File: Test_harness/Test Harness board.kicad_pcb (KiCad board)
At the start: 4 copper layers, 233 x 160 mm, 173 parts, among them U1 TCA9548APWR

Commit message: more fixes
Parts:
- RNL2_2_1: value R_Pack04 -> 1kΩ
- moved U1 23.8 mm to (152.5, 85.7), turned to 180 degrees
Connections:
- U1 pad 4: /SCL_1 -> /SDA_0
- UL1 pad 12: /Left connector/SCL -> /SCL_0
- UL1 pad 13: /Left connector/SDA -> /SDA_0
- UL2 pad 12: /Left connector/SCL -> /SCL_0
- UL2 pad 13: /Left connector/SDA -> /SDA_0
- UL3 pad 12: /Left connector/SCL -> /SCL_0
- UL3 pad 13: /Left connector/SDA -> /SDA_0
- UL4 pad 12: /Left connector/SCL -> /SCL_0
- UL4 pad 13: /Left connector/SDA -> /SDA_0
- UL5 pad 12: /Left connector/SCL -> /SCL_0
- UL5 pad 13: /Left connector/SDA -> /SDA_0
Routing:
- net /SCL_0: track 0.00 -> 103.7 mm, vias 0 -> 8
- net /Left connector/SCL: track 103.7 -> 0.00 mm, vias 8 -> 0
- net /SDA_0: track 0.00 -> 94.8 mm, vias 0 -> 5
- net /Left connector/SDA: track 94.8 -> 0.00 mm, vias 5 -> 0
- net /Left connector/D__STOP_CLK: track 39.2 -> 93.9 mm
- net /Left connector/D__RESET: track 41.6 -> 95.6 mm
- net /Left connector/D_MEMORY: track 44.2 -> 97.4 mm
- net /Left connector/D_MEMREF: track 46.8 -> 99.2 mm
- net /Left connector/D_IR1: track 50.6 -> 102.1 mm
- net /Left connector/D_IR2: track 53.5 -> 104.3 mm
- net /Left connector/D_IR3: track 55.8 -> 105.8 mm
- net /Left connector/D_XL_MDR_HI: track 58.2 -> 107.4 mm
- net /Left connector/D__PSEL1: track 60.0 -> 108.4 mm
- net /Left connector/D__RD: track 59.7 -> 107.2 mm
- net /Left connector/D__WR: track 58.9 -> 105.8 mm
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
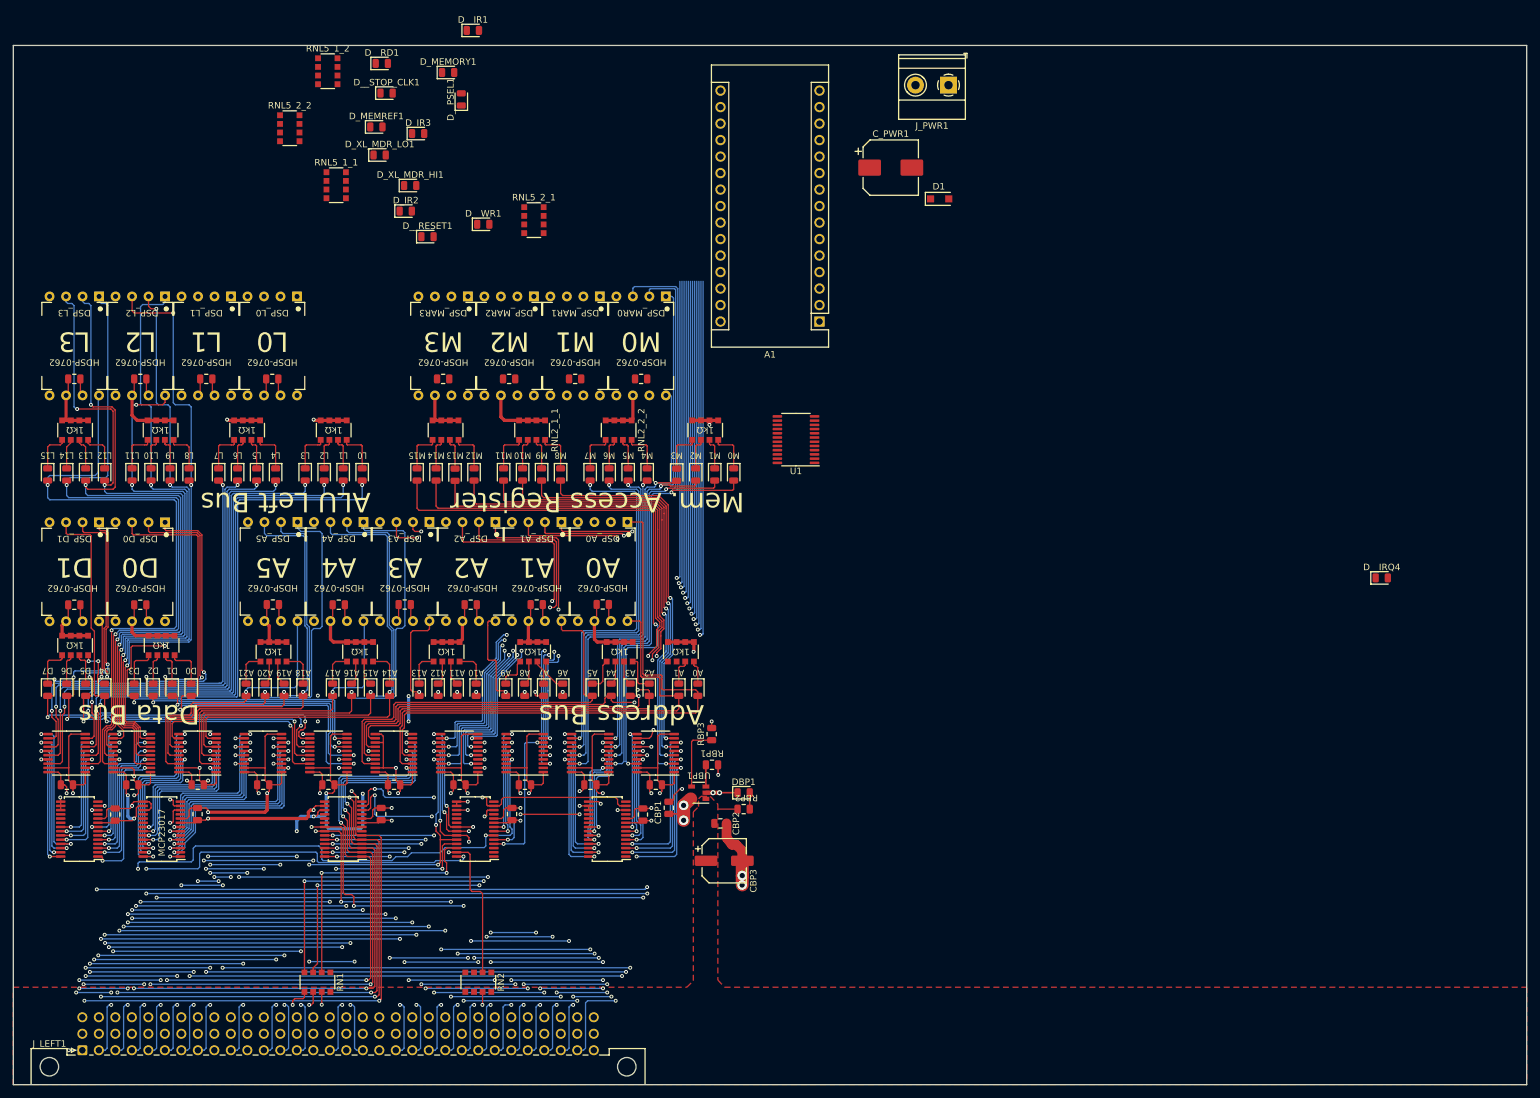
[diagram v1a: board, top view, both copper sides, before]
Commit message: position the last leds of the left side
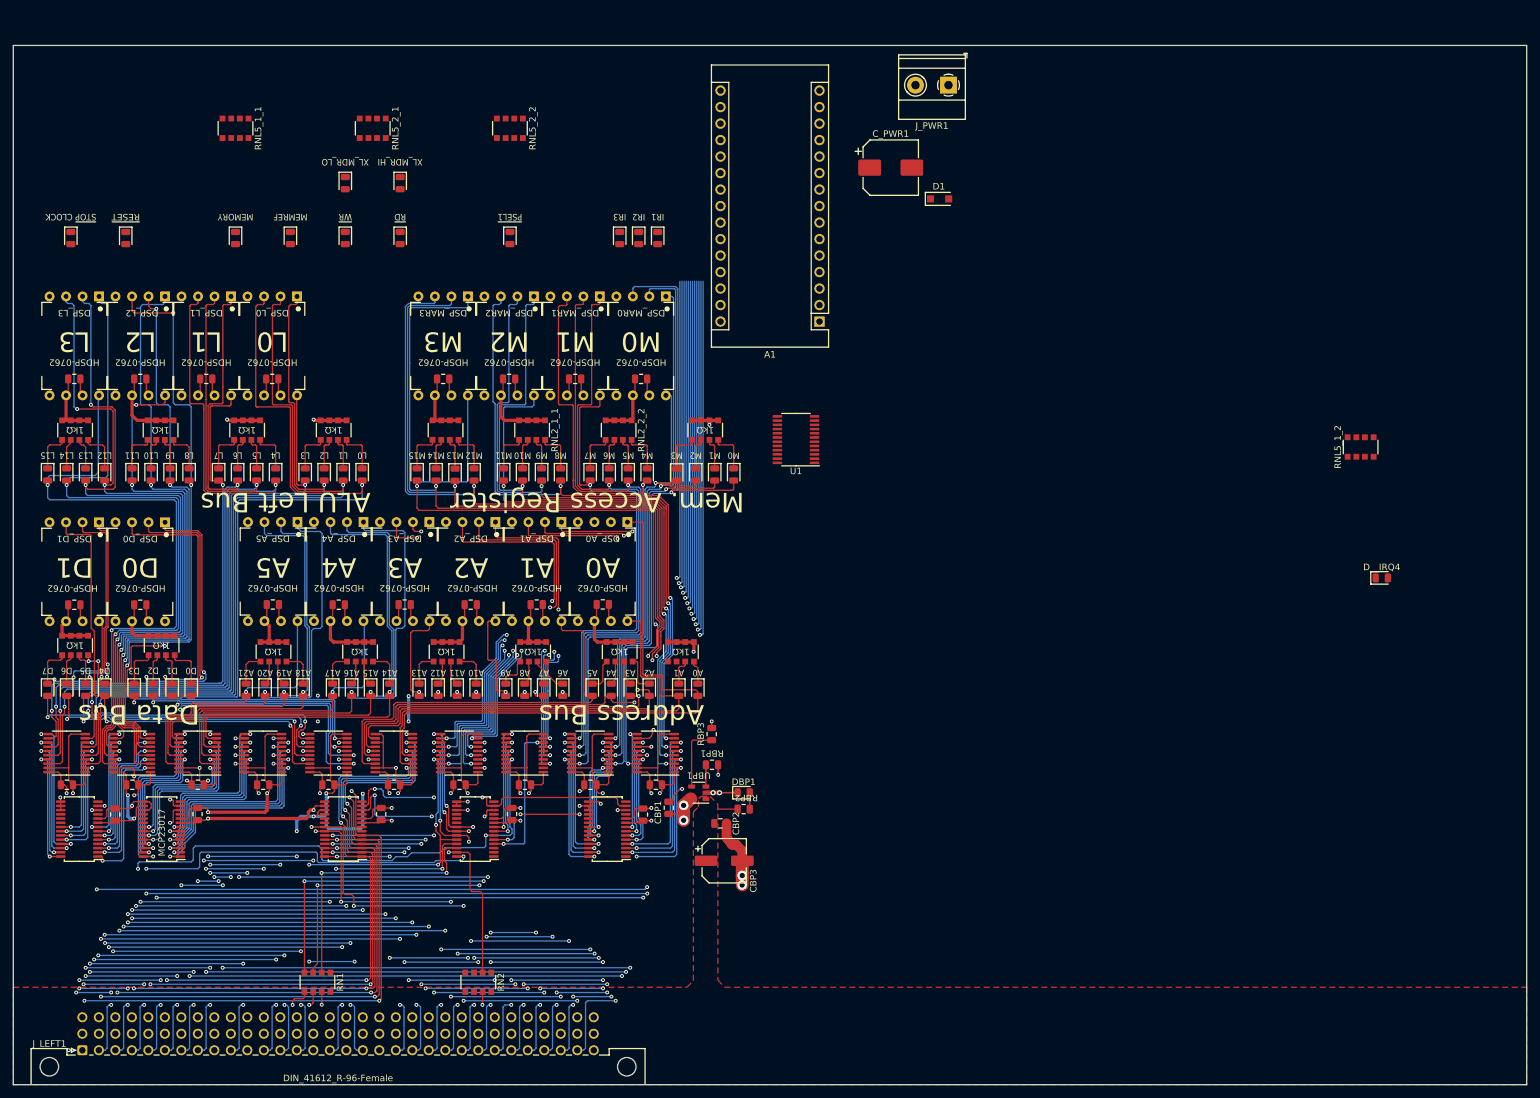
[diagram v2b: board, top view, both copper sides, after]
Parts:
- moved RNL5_1_2 169.2 mm to (239.4, 86.8), turned to 90 degrees
- moved D__STOP_CLK1 53.5 mm to (40.9, 54.6), turned to -90 degrees
- moved D__RESET1 46.5 mm to (49.3, 54.6), turned to -90 degrees
- moved D__IR1 42.8 mm to (131.2, 54.6), turned to -90 degrees
- moved D_MEMORY1 41.5 mm to (66.2, 54.6), turned to -90 degrees
- moved D_IR2 36.1 mm to (128.3, 54.6), turned to -90 degrees
- moved D_IR3 35.0 mm to (125.4, 54.6), turned to -90 degrees
- moved RNL5_2_2 33.9 mm to (108.5, 37.8), turned to -90 degrees
- moved RNL5_2_1 28.6 mm to (87.3, 37.8), turned to -90 degrees
- moved D__RD1 27.0 mm to (91.6, 54.6), turned to -90 degrees
- moved D__PSEL1 22.6 mm to (108.5, 54.6), turned to -90 degrees
- moved D_MEMREF1 21.6 mm to (74.7, 54.6), turned to -90 degrees
- moved D__WR1 21.4 mm to (83.1, 54.6), turned to -90 degrees
- moved RNL5_1_1 17.8 mm to (66.2, 37.8), turned to -90 degrees
- moved D_XL_MDR_LO1 6.84 mm to (83.1, 46.2), turned to -90 degrees
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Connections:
- RNL5_1_1 pad 5: Net-(D_MEMREF1-Pad1) -> Net-(D__STOP_CLK1-Pad1)
- RNL5_1_1 pad 6: Net-(D_MEMORY1-Pad1) -> Net-(D__RESET1-Pad1)
- RNL5_1_1 pad 7: Net-(D__RESET1-Pad1) -> Net-(D_MEMORY1-Pad1)
- RNL5_1_1 pad 8: Net-(D__STOP_CLK1-Pad1) -> Net-(D_MEMREF1-Pad1)
- RNL5_2_2 pad 5: Net-(D__IR1-Pad1) -> Net-(D_XL_MDR_HI1-Pad1)
- RNL5_2_2 pad 6: Net-(D_IR2-Pad1) -> Net-(D_IR3-Pad1)
- RNL5_2_2 pad 7: Net-(D_IR3-Pad1) -> Net-(D_IR2-Pad1)
- RNL5_2_2 pad 8: Net-(D_XL_MDR_HI1-Pad1) -> Net-(D__IR1-Pad1)
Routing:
- net /Left connector/D_L0: track 85.3 -> 133.3 mm
- net /Left connector/D_MAR12: track 70.6 -> 116.8 mm, vias 2 -> 3
- net /Left connector/D_L4: track 77.5 -> 122.6 mm
- net /Left connector/D_MAR4: track 54.2 -> 99.3 mm
- net /Left connector/D_MAR13: track 75.3 -> 119.9 mm, vias 2 -> 3
- net /Left connector/D_MAR14: track 78.6 -> 121.9 mm, vias 2 -> 3
- net /Left connector/D_MAR8: track 57.7 -> 100.3 mm, vias 2 -> 3
- net /Left connector/D_L1: track 81.5 -> 123.5 mm
- net /Left connector/D_MAR9: track 62.0 -> 102.3 mm, vias 2 -> 3
- net /Left connector/D_MAR5: track 53.9 -> 93.7 mm
- net /Left connector/D_L5: track 73.4 -> 112.9 mm
- net /Left connector/D_MAR10: track 66.3 -> 105.2 mm, vias 2 -> 3
- net /Left connector/D_MAR6: track 54.9 -> 92.8 mm
- net /Left connector/D_L6: track 69.7 -> 107.3 mm
- net /Left connector/D_L2: track 77.7 -> 113.7 mm
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
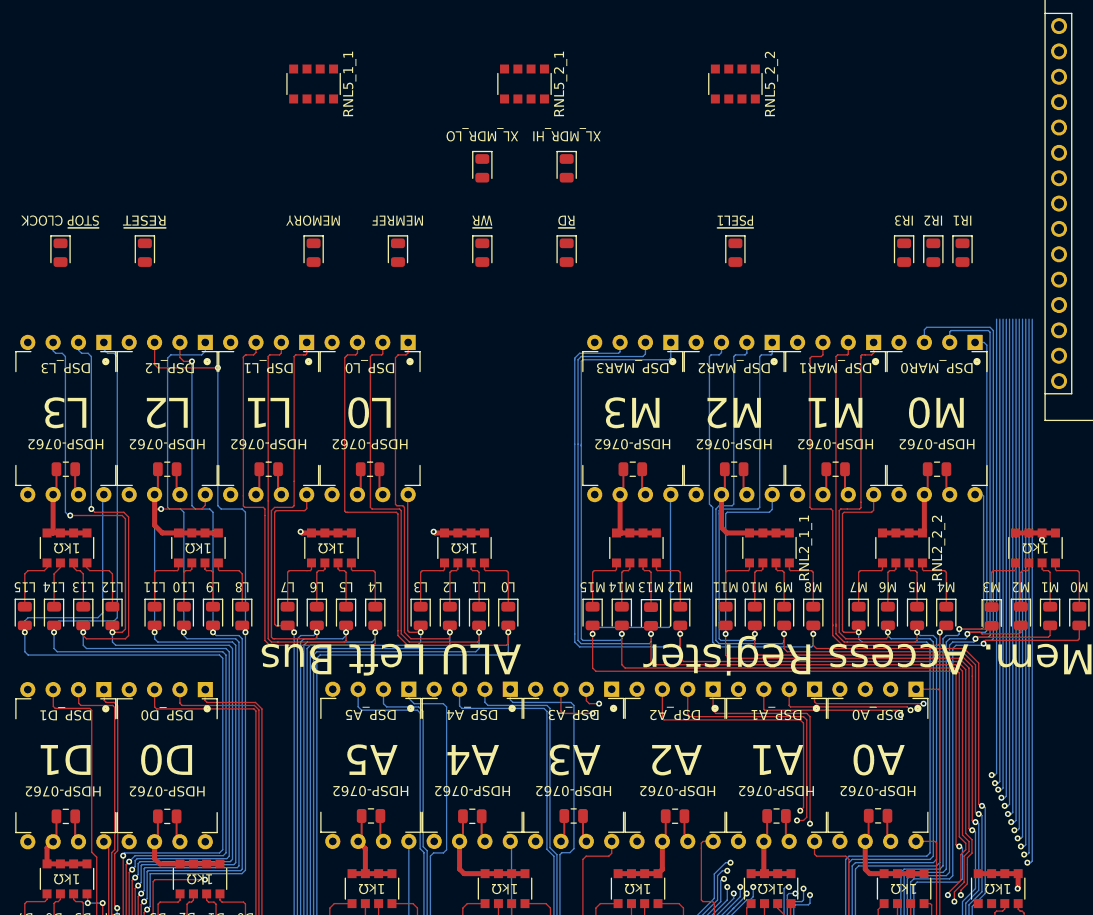
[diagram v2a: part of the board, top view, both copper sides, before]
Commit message: add memory component, fix a few things
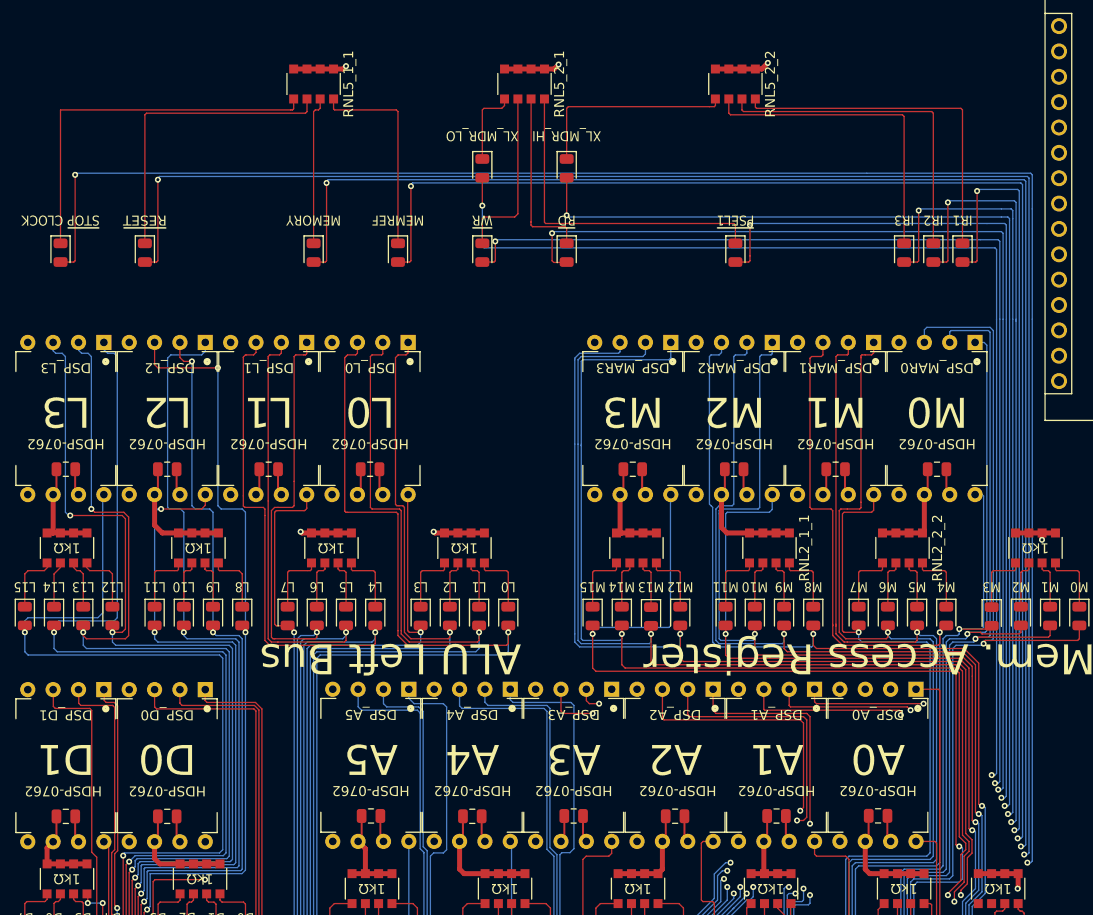
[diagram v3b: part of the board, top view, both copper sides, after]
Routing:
- net /Left connector/D__STOP_CLK: track 93.9 -> 214.5 mm, vias 3 -> 4
- net /Left connector/D__RESET: track 95.6 -> 206.8 mm, vias 3 -> 4
- net /Left connector/D_MEMORY: track 97.4 -> 190.7 mm, vias 3 -> 4
- net /Left connector/D_MEMREF: track 99.2 -> 183.0 mm, vias 3 -> 4
- net /Left connector/D_XL_MDR_LO: track 104.1 -> 169.6 mm, vias 3 -> 4
- net /Left connector/D__WR: track 105.8 -> 167.5 mm, vias 3 -> 4
- net /Left connector/D_XL_MDR_HI: track 107.4 -> 165.7 mm, vias 3 -> 4
- net /Left connector/D__RD: track 107.2 -> 165.4 mm, vias 3 -> 4
- net /Left connector/D__PSEL1: track 108.4 -> 148.7 mm, vias 3 -> 4
- net Net-(D__STOP_CLK1-Pad1): track 0.00 -> 37.7 mm
- net Net-(D__IR1-Pad1): track 0.00 -> 35.1 mm
- net Net-(D_IR2-Pad1): track 0.00 -> 33.4 mm
- net Net-(D__PSEL1-Pad1): track 0.00 -> 33.4 mm
- net Net-(D_IR3-Pad1): track 0.00 -> 31.8 mm
- net Net-(D__RESET1-Pad1): track 0.00 -> 30.5 mm
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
